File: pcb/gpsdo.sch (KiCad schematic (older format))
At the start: 25 parts

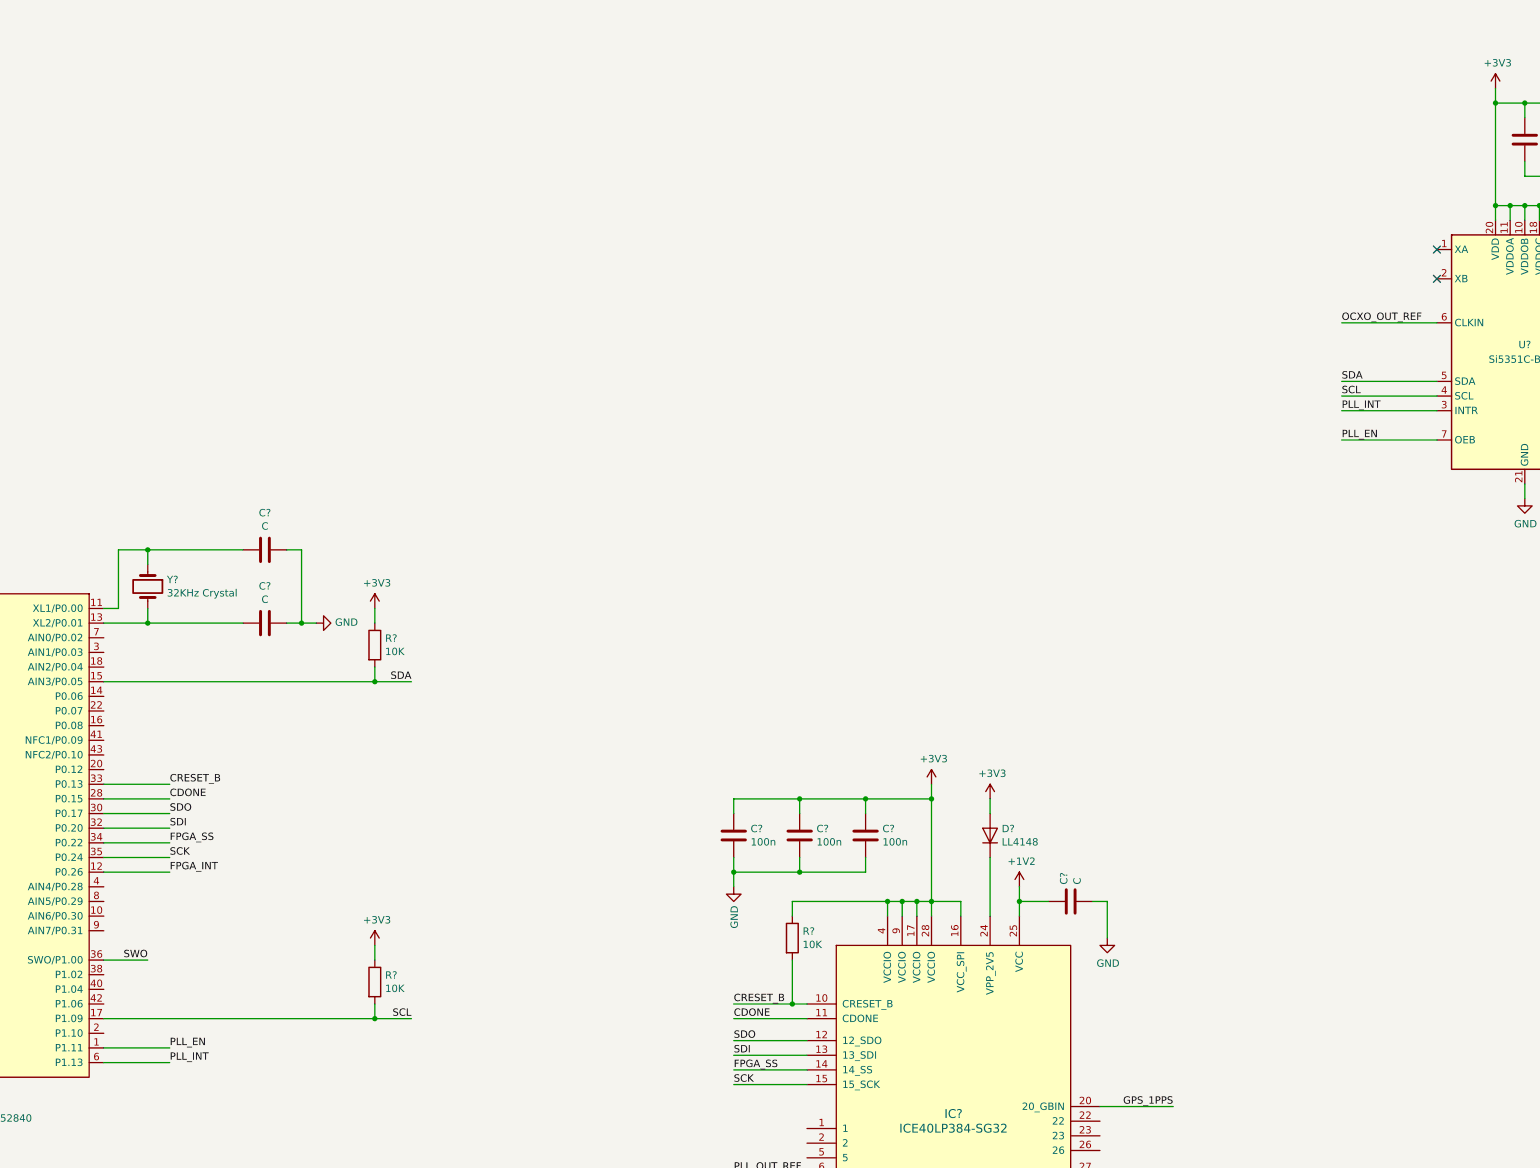
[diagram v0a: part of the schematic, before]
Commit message: add 8663-XS OCXO
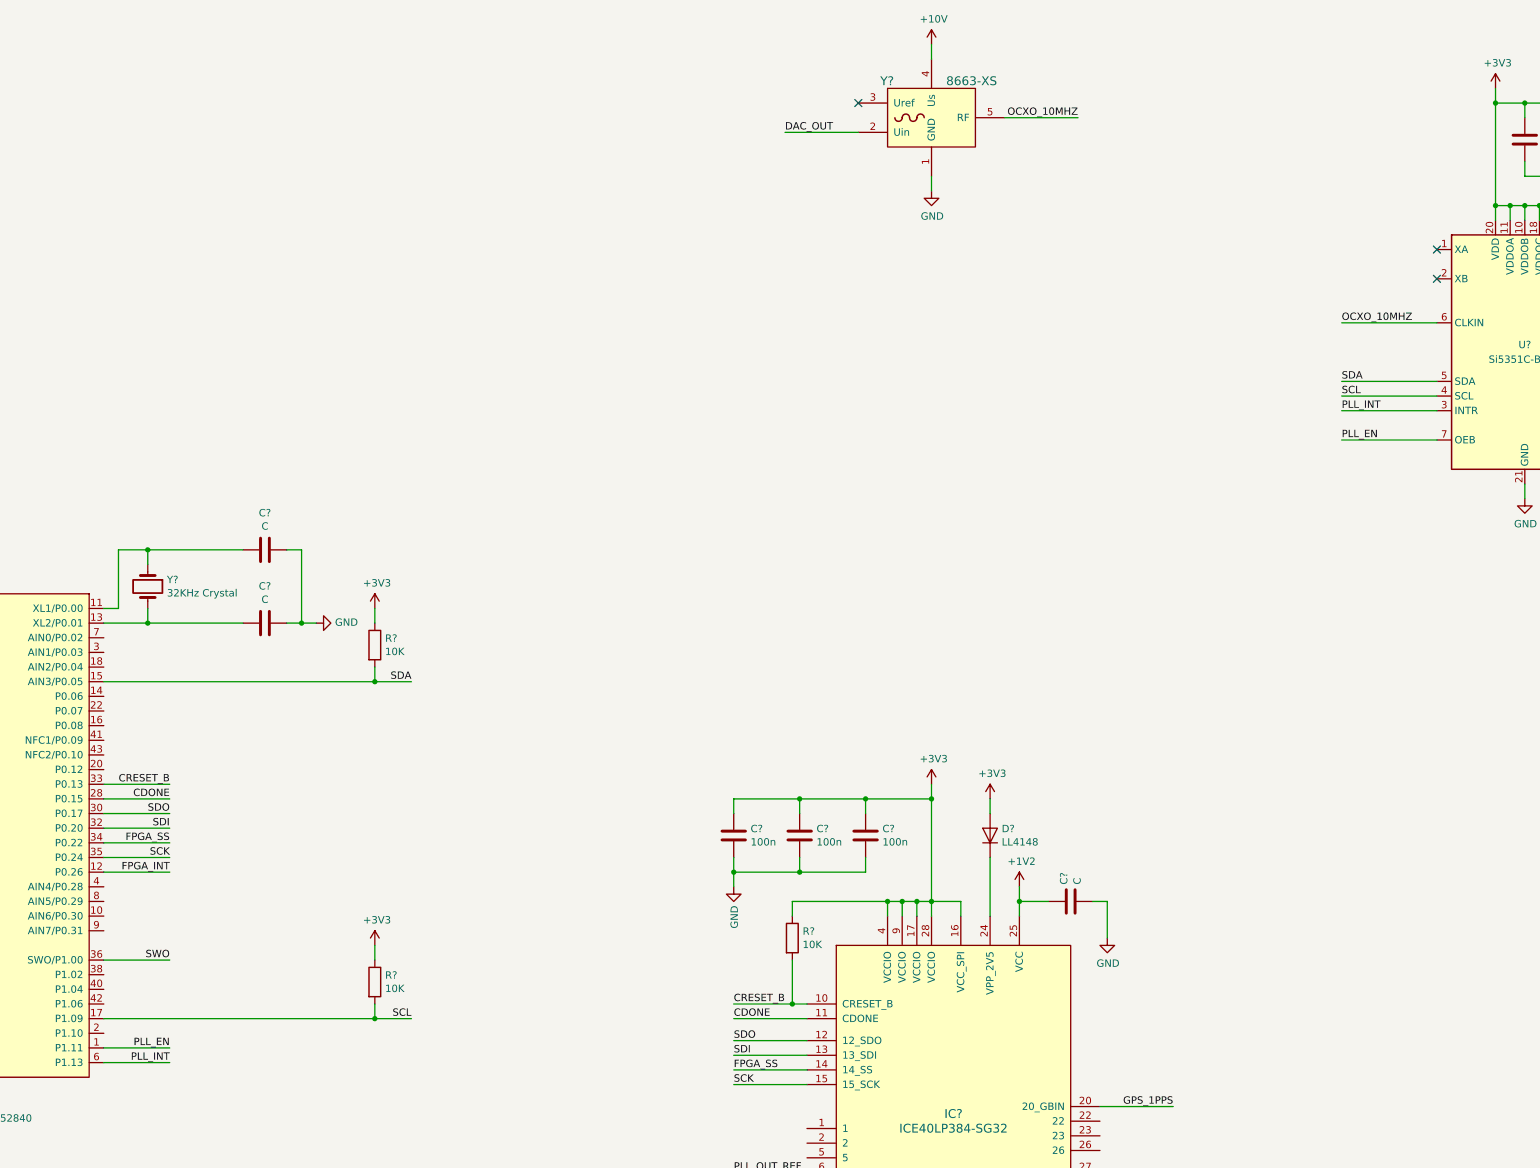
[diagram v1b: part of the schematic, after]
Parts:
- added Y?: 8663-XS, symbol oscilloquartz:8663-XS
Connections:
- net GND: now also Y?.1 (GND)
- net OCXO_OUT_REF renamed OCXO_10MHZ
- net OCXO_10MHZ: now also Y?.5 (RF)
- new net +10V: Y?.4 (Us)
- new net DAC_OUT: Y?.2 (Uin)
- no-connect marks 8 -> 9
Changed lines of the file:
@@
 ~RESET
 Wire Wire Line
-	4200 7950 4500 7950
-Text Label 4500 7950 2    50   ~ 0
+	4200 7950 4650 7950
+Text Label 4650 7950 2    50   ~ 0
 SWO
 $Comp
@@
 Wire Wire Line
 	4200 7250 4650 7250
-Text Label 4650 6950 0    50   ~ 0
+Text Label 4650 6950 2    50   ~ 0
 SDO
-Text Label 4650 7050 0    50   ~ 0
+Text Label 4650 7050 2    50   ~ 0
 SDI
-Text Label 4650 7150 0    50   ~ 0
+Text Label 4650 7150 2    50   ~ 0
 FPGA_SS
-Text Label 4650 7250 0    50   ~ 0
+Text Label 4650 7250 2    50   ~ 0
 SCK
-Text Label 4650 6850 0    50   ~ 0
+Text Label 4650 6850 2    50   ~ 0
 CDONE
-Text Label 4650 6750 0    50   ~ 0
+Text Label 4650 6750 2    50   ~ 0
 CRESET_B
 $Comp
@@
 	13300 3600 12650 3600
 Text Label 12650 3600 0    50   ~ 0
-OCXO_OUT_REF
+OCXO_10MHZ
 Wire Wire Line
 	13300 4400 12650 4400
@@
 Wire Wire Line
 	4200 8650 4650 8650
-Text Label 4650 8650 0    50   ~ 0
+Text Label 4650 8650 2    50   ~ 0
 PLL_INT
 Wire Wire Line
 	4650 8550 4200 8550
-Text Label 4650 8550 0    50   ~ 0
+Text Label 4650 8550 2    50   ~ 0
 PLL_EN
 NoConn ~ 13300 3100
@@
 Wire Wire Line
 	4200 7350 4650 7350
-Text Label 4650 7350 0    50   ~ 0
+Text Label 4650 7350 2    50   ~ 0
 FPGA_INT
+$Comp
+L oscilloquartz:8663-XS Y?
+U 1 1 5E8BB80C
+P 9850 2200
+F 0 "Y?" H 9500 2450 60  0000 L CNN
+F 1 "8663-XS" H 9950 2450 60  0000 L CNN
+F 2 "" H 9850 1850 60  0000 C CNN
+F 3 "http://www.sungwhatech.com/product/pdf/aging/8663.pdf" H 9850 1850 60  0001 C CNN
+	1    9850 2200
+	1    0    0    -1
+$EndComp
+Wire Wire Line
+	10350 2200 10850 2200
+Text Label 10850 2200 2    50   ~ 0
+OCXO_10MHZ
+$Comp
+L power:+10V #PWR?
+U 1 1 5E8E422D
+P 9850 1700
+F 0 "#PWR?" H 9850 1550 50  0001 C CNN
+F 1 "+10V" H 9865 1873 50  0000 C CNN
+F 2 "" H 9850 1700 50  0001 C CNN
+F 3 "" H 9850 1700 50  0001 C CNN
+	1    9850 1700
+	1    0    0    -1
+$EndComp
+$Comp
+L power:GND #PWR?
+U 1 1 5E8E473D
+P 9850 2700
+F 0 "#PWR?" H 9850 2450 50  0001 C CNN
+F 1 "GND" H 9855 2527 50  0000 C CNN
+F 2 "" H 9850 2700 50  0001 C CNN
+F 3 "" H 9850 2700 50  0001 C CNN
+	1    9850 2700
+	1    0    0    -1
+$EndComp
+Wire Wire Line
+	9850 1700 9850 1800
+Wire Wire Line
+	9850 2600 9850 2700
+NoConn ~ 9350 2100
+Wire Wire Line
+	9350 2300 8850 2300
+Text Label 8850 2300 0    50   ~ 0
+DAC_OUT
 $EndSCHEMATC

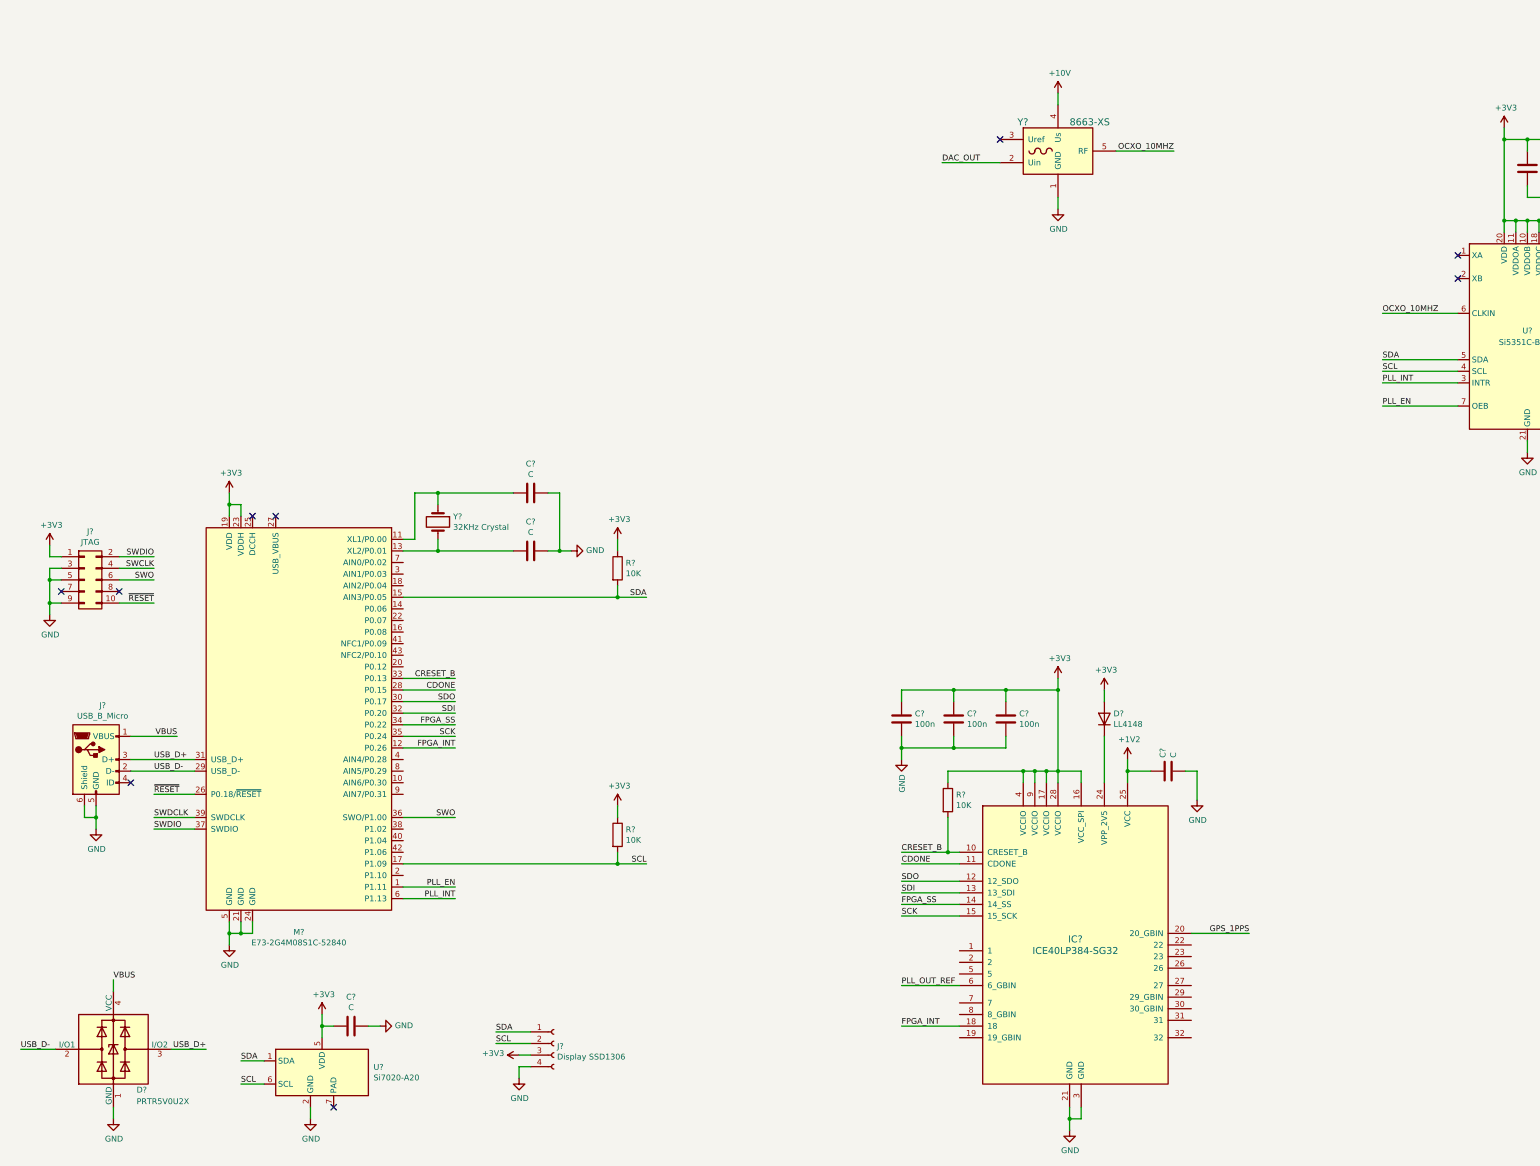
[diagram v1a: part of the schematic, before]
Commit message: add ublox NEO-7 GPS module
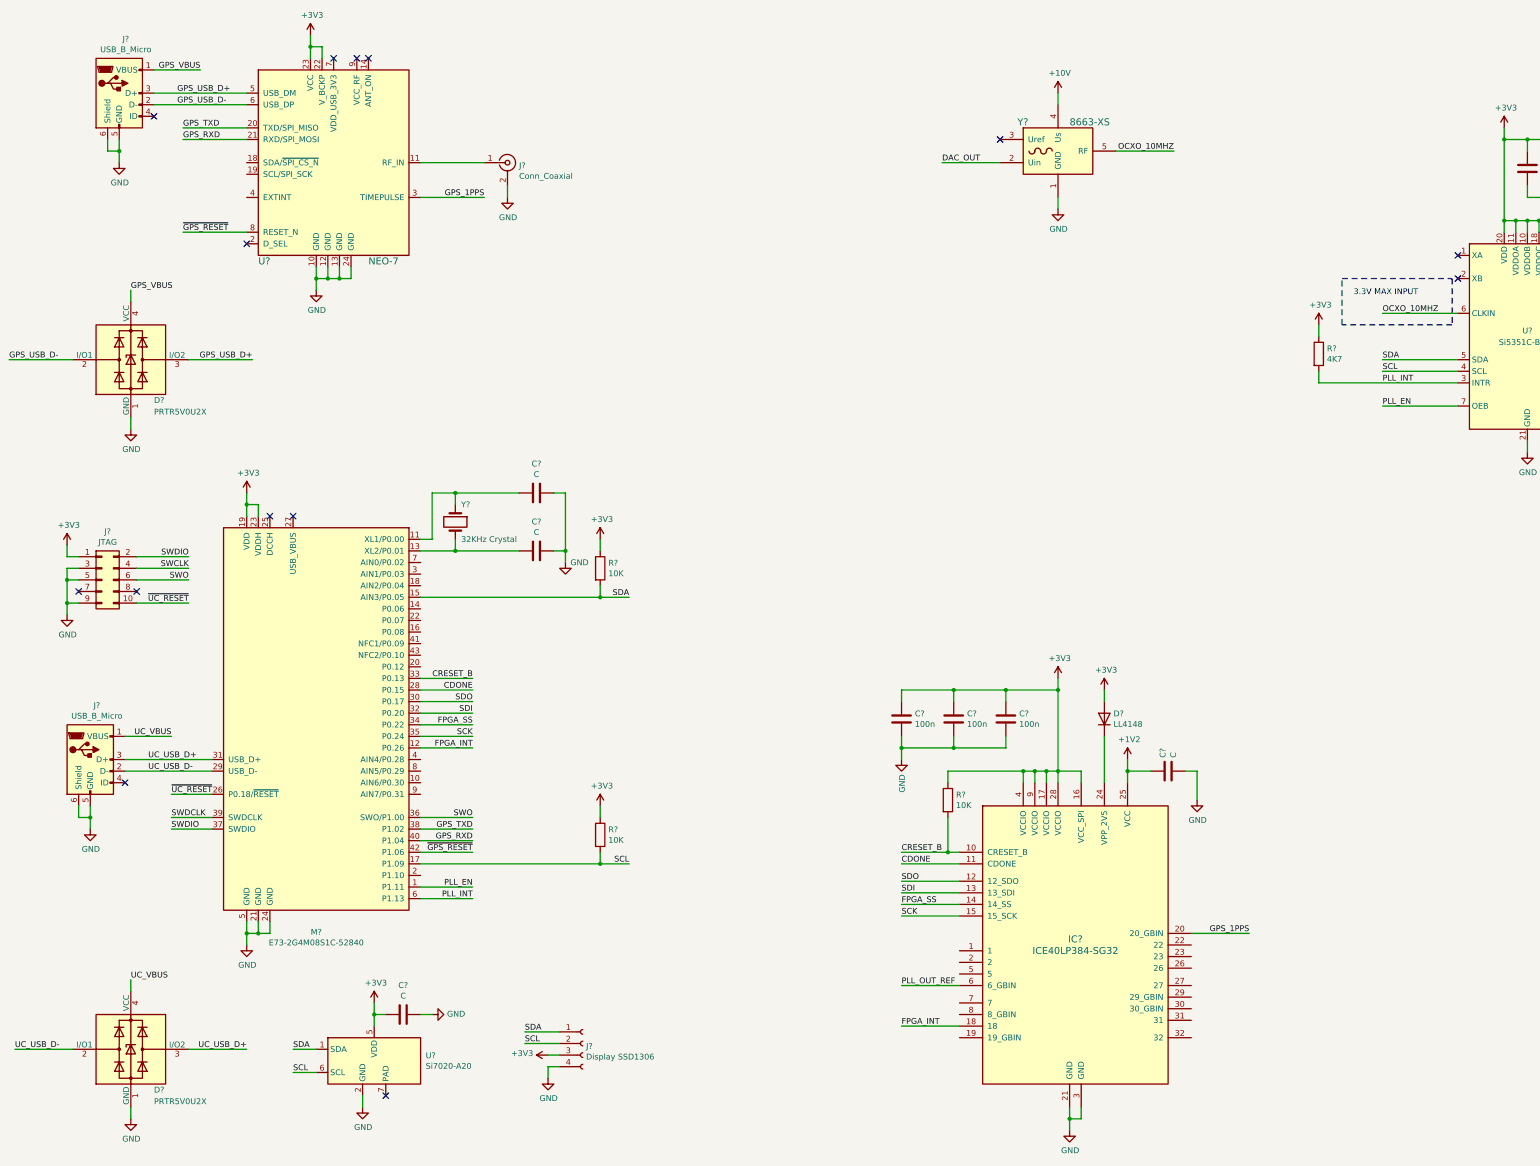
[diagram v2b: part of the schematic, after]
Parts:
- added D?: PRTR5V0U2X, Package_TO_SOT_SMD:SOT-143, symbol Power_Protection:PRTR5V0U2X
- added J?: Conn_Coaxial, symbol Connector:Conn_Coaxial
- added J?: USB_B_Micro, symbol Connector:USB_B_Micro
- added R?: 4K7, symbol Device:R
- added U?: NEO-7, symbol ublox:NEO-7
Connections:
- net +3V3: now also R?.1, U?.22 (V_BCKP), U?.23 (VCC)
- net GND: now also D?.1 (GND), J?.2 (Ext), J?.5 (GND), J?.6 (Shield), U?.10 (GND), U?.12 (GND), U?.13 (GND), U?.24 (GND)
- net GPS_1PPS: now also U?.3 (TIMEPULSE)
- net PLL_INT: now also R?.2
- net GPS_TXD: now reaches M?.38 (P1.02)
- net GPS_TXD: now also U?.20 (TXD/SPI_MISO)
- net GPS_RXD: now reaches M?.40 (P1.04)
- net GPS_RXD: now also U?.21 (RXD/SPI_MOSI)
- net ~GPS_RESET: now reaches M?.42 (P1.06)
- net ~GPS_RESET: now also U?.8 (RESET_N)
- net USB_D+ renamed UC_USB_D+
- net USB_D- renamed UC_USB_D-
- net VBUS renamed UC_VBUS
- net ~RESET renamed ~UC_RESET
- new net: J?.1 (In), U?.11 (RF_IN)
- new net GPS_USB_D+: D?.3 (I/O2), J?.3 (D+), U?.5 (USB_DM)
- new net GPS_USB_D-: D?.2 (I/O1), J?.2 (D-), U?.6 (USB_DP)
- new net GPS_VBUS: D?.4 (VCC), J?.1 (VBUS)
- no-connect marks 9 -> 14
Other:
- note added: "3.3V MAX INPUT"
- moved on the sheet: C?, D?, J?, M?, R?, U?, Y?

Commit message: schematic progress, mark areas with TODOs
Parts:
- added C?: 1n, symbol Device:C
- added R? (x2): 680, symbol Device:R
- added R? (x2): 330, symbol Device:R
- added U?: AD5761R, symbol analog_devices:AD57x1
- U?: value NEO-7 -> uBlox NEO-7M
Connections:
- net +10V: now also U?.~ (VOUT)
- net +3V3: now also U?.15 (DVCC)
- net GND: now also C?.2, R?.2, R?.2, U?.16 (DGND), U?.5 (AGND), U?.6 (VSS)
- net GPS_USB_D+: now also U?.6 (USB_DP); no longer U?.5 (USB_DM)
- net GPS_USB_D-: now also U?.5 (USB_DM); no longer U?.6 (USB_DP)
- net at Y?.3 (Uref): now also R?.1
- net OCXO_VREF: now reaches M?.3 (AIN1/P0.03)
- net OCXO_VREF: now also R?.1, R?.2
- net DAC_VAL: now reaches M?.7 (AIN0/P0.02)
- net DAC_VAL: now also R?.1, R?.2
- net DAC_OUT: no longer names the net of Y?.2 (Uin)
- net DAC_OUT: now also C?.1, R?.1, U?.~ (VOUT)
- no-connect marks 14 -> 16
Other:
- note added: "3x ENABLE?"
- note added: "LEDs?"
- note added: "OCXO input?"
- note added: "Output\nstages"
- note added: "PGOOD:\nRESET tree?"
- note added: "PSU\nTI TPS652510"
- note added: "Schmidt Trigger?"
- note added: "best practices,\nmax load?"
- note added: "buttons\nLEDs\n"
- note added: "caps?"
- note added: "control"
- note added: "interrupt"
- note added: "output voltage?"
- note added: "replace with\nmultiple\nADT7410?"
- moved on the sheet: J?, Y?

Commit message: add TPS652510, schematic progress and layout
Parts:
- removed J? (x2): USB_B_Micro, symbol Connector:USB_B_Micro
- added C? (x15): C, symbol Device:C
- added C? (x2): 10u, symbol Device:C
- added C?: 100n, symbol Device:C
- added J? (x2): USB_B_Micro, symbol Connector:USB_B_Micro
- added L? (x3): L, symbol Device:L
- added R? (x12): R, symbol Device:R
- added U?: TPS652510, symbol texas_instruments:TPS652510
- Y?: value 32KHz Crystal -> 32786Hz
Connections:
- net +10V: now also C?.1, L?.1, R?.1, R?.2
- net +1V2: now also C?.1, L?.1, R?.1, R?.2
- net +3V3: now also C?.1, L?.1, R?.1, R?.2
- net GND: now also C?.1, C?.1, C?.1, C?.1, C?.1, C?.1, C?.1, C?.1, C?.1, C?.2, C?.2, C?.2, C?.2, C?.2, C?.2, J?.5 (GND), J?.5 (GND), J?.6 (Shield), J?.6 (Shield), R?.1, R?.1, R?.1, R?.2, R?.2, R?.2, U?.26 (UCGND), U?.30 (UCGND), U?.31 (UCGND), U?.32 (UCGND), U?.33 (UCGND), U?.34 (UCGND), U?.35 (UCGND), U?.41 (PADGND), U?.5 (UCGND)
- net GPS_USB_D+: now also J?.3 (D+)
- net GPS_USB_D-: now also J?.2 (D-)
- net GPS_VBUS: now also J?.1 (VBUS)
- net UC_USB_D+: now also J?.3 (D+)
- net UC_USB_D-: now also J?.2 (D-)
- net UC_VBUS: now also J?.1 (VBUS)
- new net: C?.1, L?.2, U?.14 (LX1), U?.15 (LX1)
- new net: C?.2, U?.12 (BST1)
- new net: C?.1, L?.2, U?.16 (LX2), U?.17 (LX2)
- new net: C?.2, U?.19 (BST2)
- new net: C?.1, L?.2, U?.36 (LX3), U?.37 (LX3)
- new net: C?.2, U?.39 (BST3)
- new net: R?.2, U?.7 (FB1)
- new net: R?.2, U?.24 (FB2)
- new net: R?.2, U?.4 (FB3)
- new net: C?.2, U?.29 (V3V)
- new net: C?.2, U?.28 (V7V)
- new net: C?.2, R?.1, U?.8 (COMP1)
- new net: C?.1, R?.2 (x3)
- new net: C?.2, R?.1, U?.23 (COMP2)
- new net: C?.2, R?.1, U?.3 (COMP3)
- new net: R?.1, U?.10 (RLIM1)
- new net: C?.2, U?.9 (SS1)
- new net: R?.1, U?.21 (RLIM2)
- new net: C?.2, U?.22 (SS2)
- new net: R?.1, U?.1 (RLIM3)
- new net: C?.2, U?.2 (SS3)
- new net: C?.2, U?.11 (EN1)
- new net +12V: U?.13 (VIN1), U?.18 (VIN2), U?.38 (VIN3)
- new net EN_10V: U?.40 (EN3)
- new net EN_1V2: U?.20 (EN2)
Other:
- note added: "FPGA"
- note added: "FREQUENCY SYNTHESIZER"
- note added: "FRONT PANEL"
- note added: "GPS RECEIVER"
- note added: "MICROCONTROLLER DOMAIN"
- note added: "POWER SUPPLY"
- note added: "TUNED OCXO"
- note added: "output\nvoltage?"
- note removed: "3x ENABLE?"
- note removed: "LEDs?"
- note removed: "OCXO input?"
- note removed: "PSU\nTI TPS652510"
- note removed: "output voltage?"
- moved on the sheet: C?, D?, IC?, J?, M?, R?, U?, Y?
